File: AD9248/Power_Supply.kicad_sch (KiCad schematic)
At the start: 18 parts, among them U5 TLV70018DCKR, U7 TLV70018DCKR

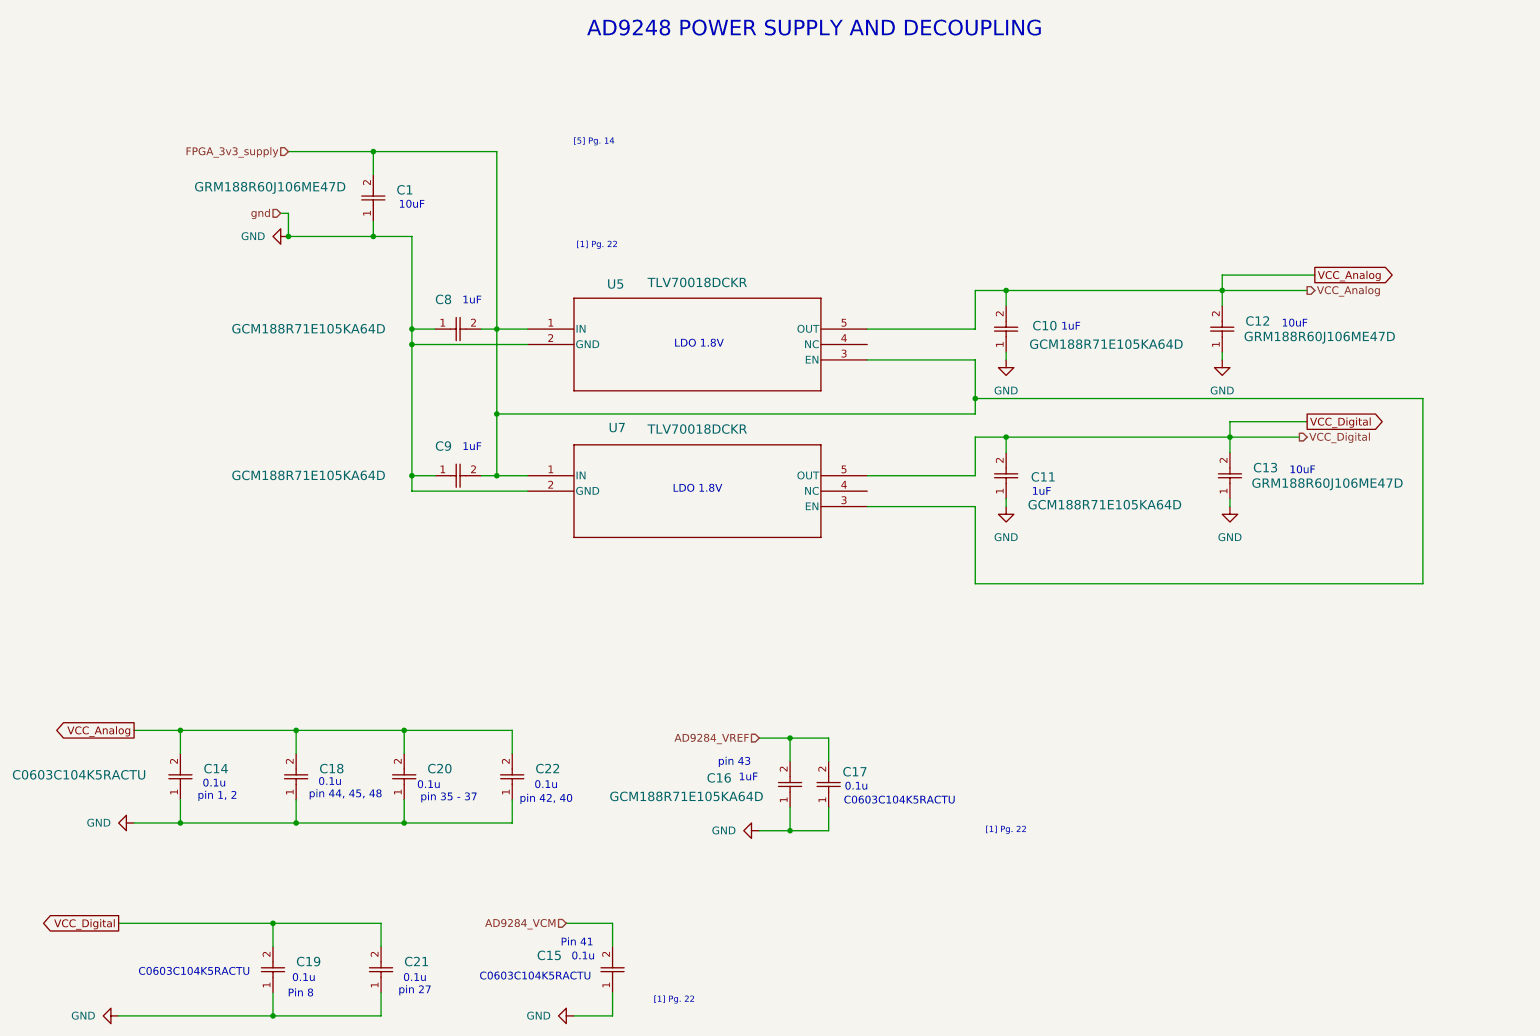
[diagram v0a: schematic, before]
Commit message: Finished and reviewed schematic, one change so far needs to be made: OE pin on level shifters must be externally toggled instead of tied to VCC. The IC requires VDDA/B to be fully ramped before pulling the OE high.
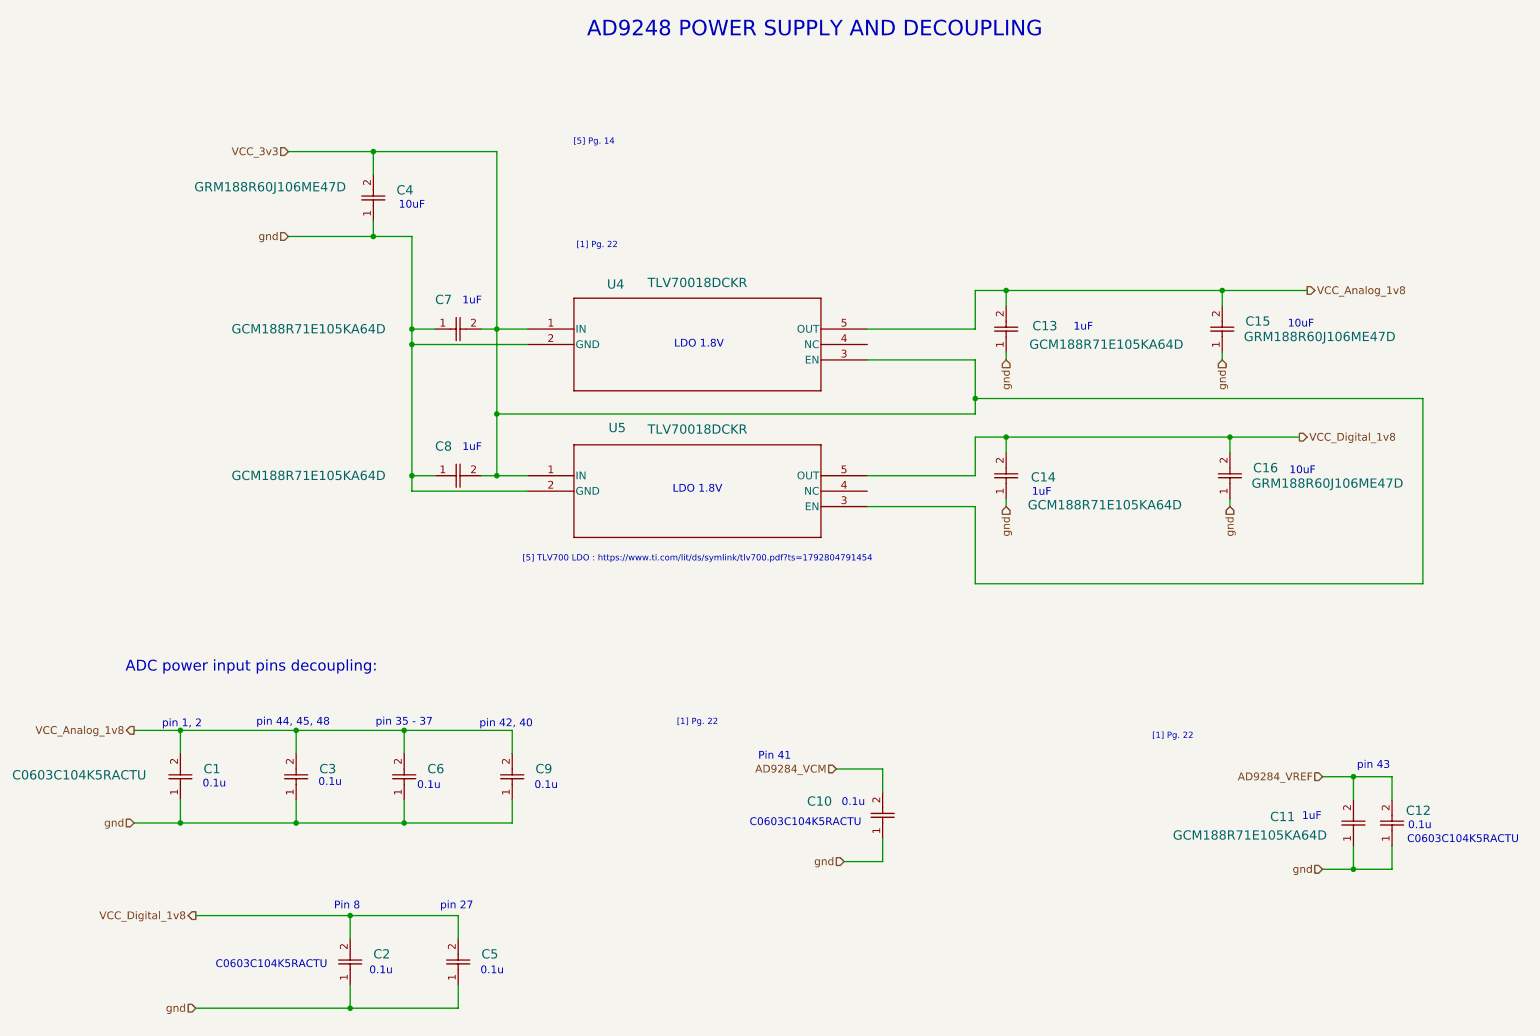
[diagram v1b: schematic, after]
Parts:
- renumbered C14 to C1, C15 to C10, C16 to C11, C17 to C12, C10 to C13, C11 to C14, C12 to C15, C13 to C16, C19 to C2, C18 to C3, C1 to C4, C21 to C5, C20 to C6, C8 to C7, C9 to C8, C22 to C9, U5 to U4, U7 to U5
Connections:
- net FPGA_3v3_supply renamed VCC_3v3
- net GND renamed gnd
- net VCC_Analog renamed VCC_Analog_1v8
- net VCC_Digital renamed VCC_Digital_1v8
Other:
- note added: "ADC power input pins decoupling:"
- note added: "[5] TLV700 LDO : https://www.ti.com/lit/ds/symlink/tlv700.pdf?ts=1792804791454"
- moved on the sheet: C10, C11, C12, C2, C5
